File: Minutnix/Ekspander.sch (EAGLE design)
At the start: 14 parts, among them X1 FH12-12S-0.5SH, X6 JST-XH-03-PIN-LONG-PAD

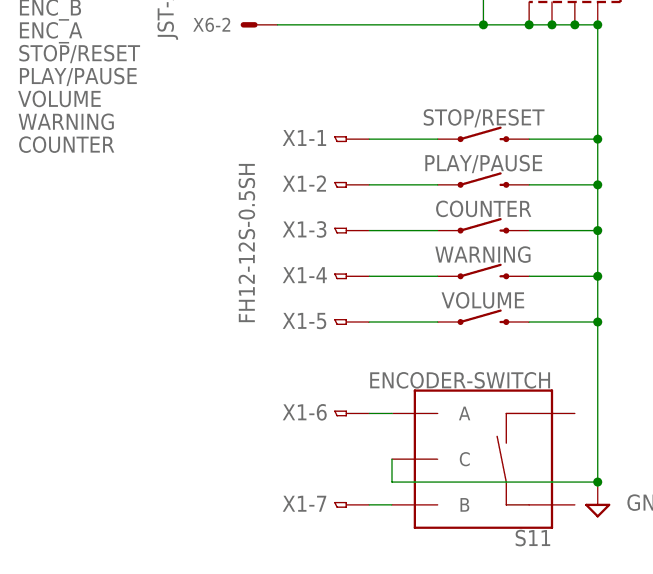
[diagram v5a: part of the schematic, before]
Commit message: libs actualisation + drc rules for expander
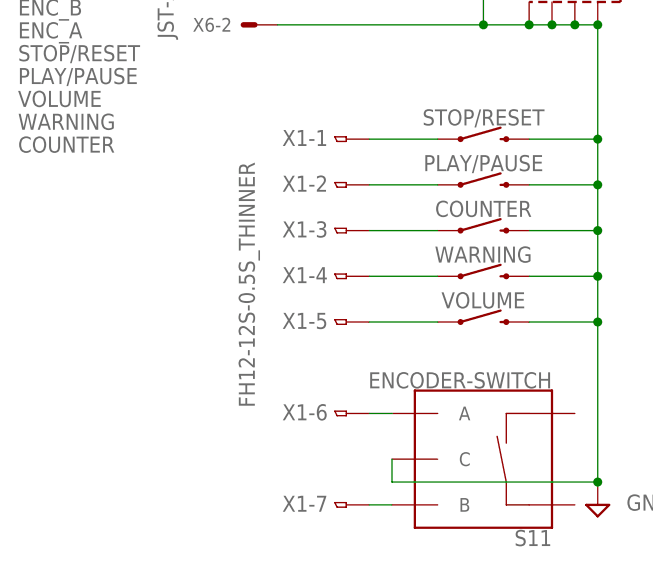
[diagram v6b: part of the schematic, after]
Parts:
- X1: value FH12-12S-0.5SH -> FH12-12S-0.5S_THINNER; device con-hirose:FH12-12S-0.5SH -> My_con-hirose:FH12-12S-0.5S_THINNER
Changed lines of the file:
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@@
 <grid distance="0.1" unitdist="inch" unit="inch" style="lines" multiple="1" display="no" altdistance="0.01" altunitdist="inch" altunit="inch"/>
 <layers>
-<layer number="1" name="Top" color="4" fill="1" visible="yes" active="no"/>
-<layer number="2" name="Route2" color="16" fill="1" visible="yes" active="no"/>
-<layer number="3" name="Route3" color="17" fill="1" visible="yes" active="no"/>
-<layer number="4" name="Route4" color="18" fill="1" visible="yes" active="no"/>
-<layer number="5" name="Route5" color="19" fill="1" visible="yes" active="no"/>
-<layer number="6" name="Route6" color="25" fill="1" visible="yes" active="no"/>
-<layer number="7" name="Route7" color="26" fill="1" visible="yes" active="no"/>
-<layer number="8" name="Route8" color="27" fill="1" visible="yes" active="no"/>
-<layer number="9" name="Route9" color="28" fill="1" visible="yes" active="no"/>
-<layer number="10" name="Route10" color="29" fill="1" visible="yes" active="no"/>
-<layer number="11" name="Route11" color="30" fill="1" visible="yes" active="no"/>
-<layer number="12" name="Route12" color="20" fill="1" visible="yes" active="no"/>
-<layer number="13" name="Route13" color="21" fill="1" visible="yes" active="no"/>
-<layer number="14" name="Route14" color="22" fill="1" visible="yes" active="no"/>
-<layer number="15" name="Route15" color="23" fill="1" visible="yes" active="no"/>
-<layer number="16" name="Bottom" color="1" fill="1" visible="yes" active="no"/>
-<layer number="17" name="Pads" color="2" fill="1" visible="yes" active="no"/>
-<layer number="18" name="Vias" color="2" fill="1" visible="yes" active="no"/>
-<layer number="19" name="Unrouted" color="6" fill="1" visible="yes" active="no"/>
-<layer number="20" name="Dimension" color="24" fill="1" visible="yes" active="no"/>
-<layer number="21" name="tPlace" color="7" fill="1" visible="yes" active="no"/>
-<layer number="22" name="bPlace" color="7" fill="1" visible="yes" active="no"/>
-<layer number="23" name="tOrigins" color="15" fill="1" visible="yes" active="no"/>
-<layer number="24" name="bOrigins" color="15" fill="1" visible="yes" active="no"/>
-<layer number="25" name="tNames" color="7" fill="1" visible="yes" active="no"/>
-<layer number="26" name="bNames" color="7" fill="1" visible="yes" active="no"/>
-<layer number="27" name="tValues" color="7" fill="1" visible="yes" active="no"/>
-<layer number="28" name="bValues" color="7" fill="1" visible="yes" active="no"/>
+<layer number="1" name="Top" color="4" fill="1" visible="no" active="no"/>
+<layer number="2" name="Route2" color="16" fill="1" visible="no" active="no"/>
+<layer number="3" name="Route3" color="17" fill="1" visible="no" active="no"/>
+<layer number="4" name="Route4" color="18" fill="1" visible="no" active="no"/>
+<layer number="5" name="Route5" color="19" fill="1" visible="no" active="no"/>
+<layer number="6" name="Route6" color="25" fill="1" visible="no" active="no"/>
+<layer number="7" name="Route7" color="26" fill="1" visible="no" active="no"/>
+<layer number="8" name="Route8" color="27" fill="1" visible="no" active="no"/>
+<layer number="9" name="Route9" color="28" fill="1" visible="no" active="no"/>
+<layer number="10" name="Route10" color="29" fill="1" visible="no" active="no"/>
+<layer number="11" name="Route11" color="30" fill="1" visible="no" active="no"/>
+<layer number="12" name="Route12" color="20" fill="1" visible="no" active="no"/>
+<layer number="13" name="Route13" color="21" fill="1" visible="no" active="no"/>
+<layer number="14" name="Route14" color="22" fill="1" visible="no" active="no"/>
+<layer number="15" name="Route15" color="23" fill="1" visible="no" active="no"/>
+<layer number="16" name="Bottom" color="1" fill="1" visible="no" active="no"/>
+<layer number="17" name="Pads" color="2" fill="1" visible="no" active="no"/>
+<layer number="18" name="Vias" color="2" fill="1" visible="no" active="no"/>
+<layer number="19" name="Unrouted" color="6" fill="1" visible="no" active="no"/>
+<layer number="20" name="Dimension" color="24" fill="1" visible="no" active="no"/>
+<layer number="21" name="tPlace" color="7" fill="1" visible="no" active="no"/>
+<layer number="22" name="bPlace" color="7" fill="1" visible="no" active="no"/>
+<layer number="23" name="tOrigins" color="15" fill="1" visible="no" active="no"/>
+<layer number="24" name="bOrigins" color="15" fill="1" visible="no" active="no"/>
+<layer number="25" name="tNames" color="7" fill="1" visible="no" active="no"/>
+<layer number="26" name="bNames" color="7" fill="1" visible="no" active="no"/>
+<layer number="27" name="tValues" color="7" fill="1" visible="no" active="no"/>
+<layer number="28" name="bValues" color="7" fill="1" visible="no" active="no"/>
 <layer number="29" name="tStop" color="7" fill="3" visible="no" active="no"/>
 <layer number="30" name="bStop" color="7" fill="6" visible="no" active="no"/>
@@
 <layer number="35" name="tGlue" color="7" fill="4" visible="no" active="no"/>
 <layer number="36" name="bGlue" color="7" fill="5" visible="no" active="no"/>
-<layer number="37" name="tTest" color="7" fill="1" visible="yes" active="no"/>
-<layer number="38" name="bTest" color="7" fill="1" visible="yes" active="no"/>
+<layer number="37" name="tTest" color="7" fill="1" visible="no" active="no"/>
+<layer number="38" name="bTest" color="7" fill="1" visible="no" active="no"/>
 <layer number="39" name="tKeepout" color="4" fill="11" visible="no" active="no"/>
 <layer number="40" name="bKeepout" color="1" fill="11" visible="no" active="no"/>
@@
 <layer number="44" name="Drills" color="7" fill="1" visible="no" active="no"/>
 <layer number="45" name="Holes" color="7" fill="1" visible="no" active="no"/>
-<layer number="46" name="Milling" color="3" fill="1" visible="yes" active="no"/>
-<layer number="47" name="Measures" color="7" fill="1" visible="yes" active="no"/>
-<layer number="48" name="Document" color="7" fill="1" visible="yes" active="no"/>
-<layer number="49" name="Reference" color="7" fill="1" visible="yes" active="no"/>
-<layer number="50" name="dxf" color="7" fill="1" visible="yes" active="no"/>
-<layer number="51" name="tDocu" color="7" fill="1" visible="yes" active="no"/>
-<layer number="52" name="bDocu" color="7" fill="1" visible="yes" active="no"/>
-<layer number="53" name="tGND_GNDA" color="7" fill="9" visible="yes" active="no"/>
-<layer number="54" name="bGND_GNDA" color="1" fill="9" visible="yes" active="no"/>
-<layer number="56" name="wert" color="7" fill="1" visible="yes" active="no"/>
-<layer number="57" name="tCAD" color="7" fill="1" visible="yes" active="no"/>
-<layer number="59" name="tCarbon" color="7" fill="1" visible="yes" active="no"/>
-<layer number="60" name="bCarbon" color="7" fill="1" visible="yes" active="no"/>
+<layer number="46" name="Milling" color="3" fill="1" visible="no" active="no"/>
+<layer number="47" name="Measures" color="7" fill="1" visible="no" active="no"/>
+<layer number="48" name="Document" color="7" fill="1" visible="no" active="no"/>
+<layer number="49" name="Reference" color="7" fill="1" visible="no" active="no"/>
+<layer number="50" name="dxf" color="7" fill="1" visible="no" active="no"/>
+<layer number="51" name="tDocu" color="7" fill="1" visible="no" active="no"/>
+<layer number="52" name="bDocu" color="7" fill="1" visible="no" active="no"/>
+<layer number="53" name="tGND_GNDA" color="7" fill="9" visible="no" active="no"/>
+<layer number="54" name="bGND_GNDA" color="1" fill="9" visible="no" active="no"/>
+<layer number="56" name="wert" color="7" fill="1" visible="no" active="no"/>
+<layer number="57" name="tCAD" color="7" fill="1" visible="no" active="no"/>
+<layer number="59" name="tCarbon" color="7" fill="1" visible="no" active="no"/>
+<layer number="60" name="bCarbon" color="7" fill="1" visible="no" active="no"/>
 <layer number="88" name="SimResults" color="9" fill="1" visible="yes" active="yes"/>
 <layer number="89" name="SimProbes" color="9" fill="1" visible="yes" active="yes"/>
@@
 <part name="S11" library="SparkFun-Switches" library_urn="urn:adsk.eagle:library:535" deviceset="ENCODER-SWITCH" device="" package3d_urn="urn:adsk.eagle:package:40158/1"/>
 <part name="L_WARNING" library="led" library_urn="urn:adsk.eagle:library:259" deviceset="LED" device="CHIPLED_0805" package3d_urn="urn:adsk.eagle:package:15821/2"/>
-<part name="X1" library="con-hirose" library_urn="urn:adsk.eagle:library:152" deviceset="FH12-12S-0.5S" device="H" package3d_urn="urn:adsk.eagle:package:7320/1"/>
+<part name="X1" library="My_con-hirose" deviceset="FH12-12S-0.5S_THINNER" device=""/>
 <part name="SUPPLY1" library="supply2" library_urn="urn:adsk.eagle:library:372" deviceset="GND" device=""/>
 <part name="SUPPLY7" library="supply2" library_urn="urn:adsk.eagle:library:372" deviceset="+5V" device=""/>
@@
 </sheet>
 </sheets>
+<errors>
+</errors>
 </schematic>
 </drawing>

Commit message: Probably final routing of Expander board
DRC 8mils clean
libs actualisation
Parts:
- COUNTER, PLAY/PAUSE, STOP/RESET, VOLUME, WARNING: device SparkFun-Switches:MOMENTARY-SWITCH-SPST-PTH-12MM -> MySparkFun-Switches:MOMENTARY-SWITCH-SPST-PTH-12MM
- S11: device SparkFun-Switches:ENCODER-SWITCH -> MySparkFun-Switches:ENCODER-SWITCH
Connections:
- net +5V: now also S11.SW-
- net GND: now also COUNTER.4, PLAY/PAUSE.4, S11.GND1, S11.GND2, S11.SW+, STOP/RESET.4, VOLUME.4, WARNING.4
- net N$2: now also STOP/RESET.3
- net N$3: now also PLAY/PAUSE.3
- net N$4: now also COUNTER.3
- net N$5: now also WARNING.3
- net N$6: now also VOLUME.3
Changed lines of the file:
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@@
 </classes>
 <parts>
-<part name="S11" library="SparkFun-Switches" library_urn="urn:adsk.eagle:library:535" deviceset="ENCODER-SWITCH" device="" package3d_urn="urn:adsk.eagle:package:40158/1"/>
+<part name="S11" library="MySparkFun-Switches" deviceset="ENCODER-SWITCH" device="" package3d_urn="urn:adsk.eagle:package:40158/1"/>
 <part name="L_WARNING" library="led" library_urn="urn:adsk.eagle:library:259" deviceset="LED" device="CHIPLED_0805" package3d_urn="urn:adsk.eagle:package:15821/2"/>
 <part name="X1" library="My_con-hirose" deviceset="FH12-12S-0.5S_THINNER" device=""/>
@@
 <part name="L1" library="rcl" library_urn="urn:adsk.eagle:library:334" deviceset="R-EU_" device="R0603" package3d_urn="urn:adsk.eagle:package:23555/3" value="Bead"/>
 <part name="C4" library="rcl" library_urn="urn:adsk.eagle:library:334" deviceset="C-EU" device="C0603" package3d_urn="urn:adsk.eagle:package:23616/2" value="10n'"/>
-<part name="COUNTER" library="SparkFun-Switches" library_urn="urn:adsk.eagle:library:535" deviceset="MOMENTARY-SWITCH-SPST" device="-PTH-12MM" package3d_urn="urn:adsk.eagle:package:40164/1"/>
-<part name="WARNING" library="SparkFun-Switches" library_urn="urn:adsk.eagle:library:535" deviceset="MOMENTARY-SWITCH-SPST" device="-PTH-12MM" package3d_urn="urn:adsk.eagle:package:40164/1"/>
-<part name="VOLUME" library="SparkFun-Switches" library_urn="urn:adsk.eagle:library:535" deviceset="MOMENTARY-SWITCH-SPST" device="-PTH-12MM" package3d_urn="urn:adsk.eagle:package:40164/1"/>
-<part name="PLAY/PAUSE" library="SparkFun-Switches" library_urn="urn:adsk.eagle:library:535" deviceset="MOMENTARY-SWITCH-SPST" device="-PTH-12MM" package3d_urn="urn:adsk.eagle:package:40164/1"/>
-<part name="STOP/RESET" library="SparkFun-Switches" library_urn="urn:adsk.eagle:library:535" deviceset="MOMENTARY-SWITCH-SPST" device="-PTH-12MM" package3d_urn="urn:adsk.eagle:package:40164/1"/>
+<part name="COUNTER" library="MySparkFun-Switches" deviceset="MOMENTARY-SWITCH-SPST" device="-PTH-12MM" package3d_urn="urn:adsk.eagle:package:40164/1"/>
+<part name="WARNING" library="MySparkFun-Switches" deviceset="MOMENTARY-SWITCH-SPST" device="-PTH-12MM" package3d_urn="urn:adsk.eagle:package:40164/1"/>
+<part name="VOLUME" library="MySparkFun-Switches" deviceset="MOMENTARY-SWITCH-SPST" device="-PTH-12MM" package3d_urn="urn:adsk.eagle:package:40164/1"/>
+<part name="PLAY/PAUSE" library="MySparkFun-Switches" deviceset="MOMENTARY-SWITCH-SPST" device="-PTH-12MM" package3d_urn="urn:adsk.eagle:package:40164/1"/>
+<part name="STOP/RESET" library="MySparkFun-Switches" deviceset="MOMENTARY-SWITCH-SPST" device="-PTH-12MM" package3d_urn="urn:adsk.eagle:package:40164/1"/>
 <part name="SUPPLY20" library="supply2" library_urn="urn:adsk.eagle:library:372" deviceset="VCC" device=""/>
 <part name="U$1" library="con-molex-usb" deviceset="MICRO-USB-RECEPTACLE" device=""/>
@@
 <part name="L_COUNTER" library="led" library_urn="urn:adsk.eagle:library:259" deviceset="LED" device="CHIPLED_0805" package3d_urn="urn:adsk.eagle:package:15821/2"/>
 <part name="L_VOLUME" library="led" library_urn="urn:adsk.eagle:library:259" deviceset="LED" device="CHIPLED_0805" package3d_urn="urn:adsk.eagle:package:15821/2"/>
+<part name="SUPPLY2" library="supply2" library_urn="urn:adsk.eagle:library:372" deviceset="+5V" device=""/>
 </parts>
 <sheets>
@@
 <attribute name="VALUE" x="74.168" y="196.215" size="1.778" layer="96" rot="MR180"/>
 </instance>
+<instance part="SUPPLY2" gate="+5V" x="91.44" y="109.22" smashed="yes" rot="MR0">
+<attribute name="VALUE" x="90.805" y="116.205" size="1.778" layer="96" rot="MR270"/>
+</instance>
 </instances>
 <busses>
@@
 <junction x="58.42" y="167.64"/>
 </segment>
+<segment>
+<pinref part="SUPPLY2" gate="+5V" pin="+5V"/>
+<pinref part="S11" gate="G$1" pin="SW-"/>
+</segment>
 </net>
 <net name="GND" class="0">
@@
 <wire x1="93.98" y1="127" x2="93.98" y2="121.92" width="0.1524" layer="91"/>
 <wire x1="93.98" y1="121.92" x2="93.98" y2="116.84" width="0.1524" layer="91"/>
-<wire x1="93.98" y1="116.84" x2="93.98" y2="99.06" width="0.1524" layer="91"/>
-<wire x1="71.12" y1="99.06" x2="93.98" y2="99.06" width="0.1524" layer="91"/>
+<wire x1="93.98" y1="116.84" x2="93.98" y2="114.3" width="0.1524" layer="91"/>
+<wire x1="93.98" y1="114.3" x2="93.98" y2="99.06" width="0.1524" layer="91"/>
+<wire x1="71.12" y1="99.06" x2="91.44" y2="99.06" width="0.1524" layer="91"/>
 <pinref part="S11" gate="G$1" pin="C"/>
+<wire x1="91.44" y1="99.06" x2="93.98" y2="99.06" width="0.1524" layer="91"/>
 <wire x1="71.12" y1="101.6" x2="71.12" y2="99.06" width="0.1524" layer="91"/>
 <pinref part="SUPPLY1" gate="GND" pin="GND"/>
@@
 <wire x1="86.36" y1="132.08" x2="93.98" y2="132.08" width="0.1524" layer="91"/>
 <junction x="93.98" y="132.08"/>
+<pinref part="S11" gate="G$1" pin="GND1"/>
+<wire x1="76.2" y1="114.3" x2="78.74" y2="114.3" width="0.1524" layer="91"/>
+<junction x="93.98" y="114.3"/>
+<pinref part="S11" gate="G$1" pin="GND2"/>
+<wire x1="78.74" y1="114.3" x2="93.98" y2="114.3" width="0.1524" layer="91"/>
+<junction x="78.74" y="114.3"/>
+<pinref part="VOLUME" gate="G$1" pin="4"/>
+<wire x1="86.36" y1="119.38" x2="86.36" y2="116.84" width="0.1524" layer="91"/>
+<junction x="86.36" y="116.84"/>
+<pinref part="WARNING" gate="G$1" pin="4"/>
+<wire x1="86.36" y1="124.46" x2="86.36" y2="121.92" width="0.1524" layer="91"/>
+<junction x="86.36" y="121.92"/>
+<pinref part="COUNTER" gate="G$1" pin="4"/>
+<wire x1="86.36" y1="129.54" x2="86.36" y2="127" width="0.1524" layer="91"/>
+<junction x="86.36" y="127"/>
+<pinref part="PLAY/PAUSE" gate="G$1" pin="4"/>
+<wire x1="86.36" y1="134.62" x2="86.36" y2="132.08" width="0.1524" layer="91"/>
+<junction x="86.36" y="132.08"/>
+<pinref part="STOP/RESET" gate="G$1" pin="4"/>
+<wire x1="86.36" y1="139.7" x2="86.36" y2="137.16" width="0.1524" layer="91"/>
+<junction x="86.36" y="137.16"/>
+<pinref part="S11" gate="G$1" pin="SW+"/>
+<wire x1="91.44" y1="96.52" x2="91.44" y2="99.06" width="0.1524" layer="91"/>
+<junction x="91.44" y="99.06"/>
 </segment>
 </net>
@@
 <pinref part="COUNTER" gate="G$1" pin="1"/>
 <wire x1="68.58" y1="127" x2="76.2" y2="127" width="0.1524" layer="91"/>
+<pinref part="COUNTER" gate="G$1" pin="3"/>
+<wire x1="76.2" y1="129.54" x2="76.2" y2="127" width="0.1524" layer="91"/>
+<junction x="76.2" y="127"/>
 </segment>
 </net>
@@
 <pinref part="WARNING" gate="G$1" pin="1"/>
 <wire x1="68.58" y1="121.92" x2="76.2" y2="121.92" width="0.1524" layer="91"/>
+<pinref part="WARNING" gate="G$1" pin="3"/>
+<wire x1="76.2" y1="124.46" x2="76.2" y2="121.92" width="0.1524" layer="91"/>
+<junction x="76.2" y="121.92"/>
 </segment>
 </net>
@@
 <pinref part="VOLUME" gate="G$1" pin="1"/>
 <wire x1="68.58" y1="116.84" x2="76.2" y2="116.84" width="0.1524" layer="91"/>
+<pinref part="VOLUME" gate="G$1" pin="3"/>
+<wire x1="76.2" y1="119.38" x2="76.2" y2="116.84" width="0.1524" layer="91"/>
+<junction x="76.2" y="116.84"/>
 </segment>
 </net>
@@
 <pinref part="STOP/RESET" gate="G$1" pin="1"/>
 <wire x1="68.58" y1="137.16" x2="76.2" y2="137.16" width="0.1524" layer="91"/>
+<pinref part="STOP/RESET" gate="G$1" pin="3"/>
+<wire x1="76.2" y1="139.7" x2="76.2" y2="137.16" width="0.1524" layer="91"/>
+<junction x="76.2" y="137.16"/>
 </segment>
 </net>
@@
 <pinref part="PLAY/PAUSE" gate="G$1" pin="1"/>
 <wire x1="68.58" y1="132.08" x2="76.2" y2="132.08" width="0.1524" layer="91"/>
-</segment>
-</net>
+<pinref part="PLAY/PAUSE" gate="G$1" pin="3"/>
+<wire x1="76.2" y1="134.62" x2="76.2" y2="132.08" width="0.1524" layer="91"/>
+<junction x="76.2" y="132.08"/>
+</segment>
+</net>
